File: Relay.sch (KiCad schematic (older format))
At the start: 0 parts

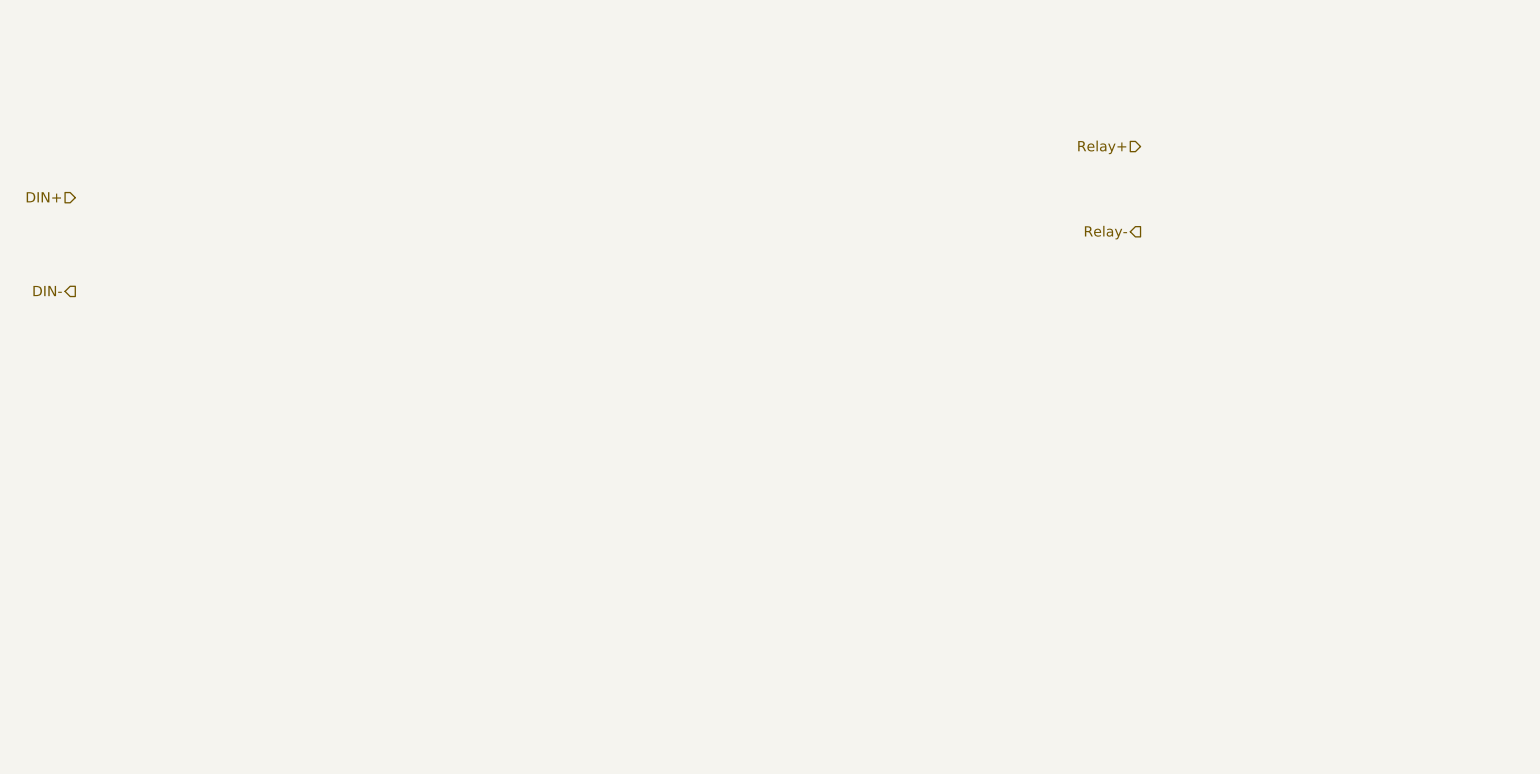
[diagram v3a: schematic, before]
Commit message: Added Relay Module Block Diagram
Everything we'll need for the relay block module, including opto and
transistor. Also created general library of schematic symbols to be used
for this project only (BenchBuddy.lib)
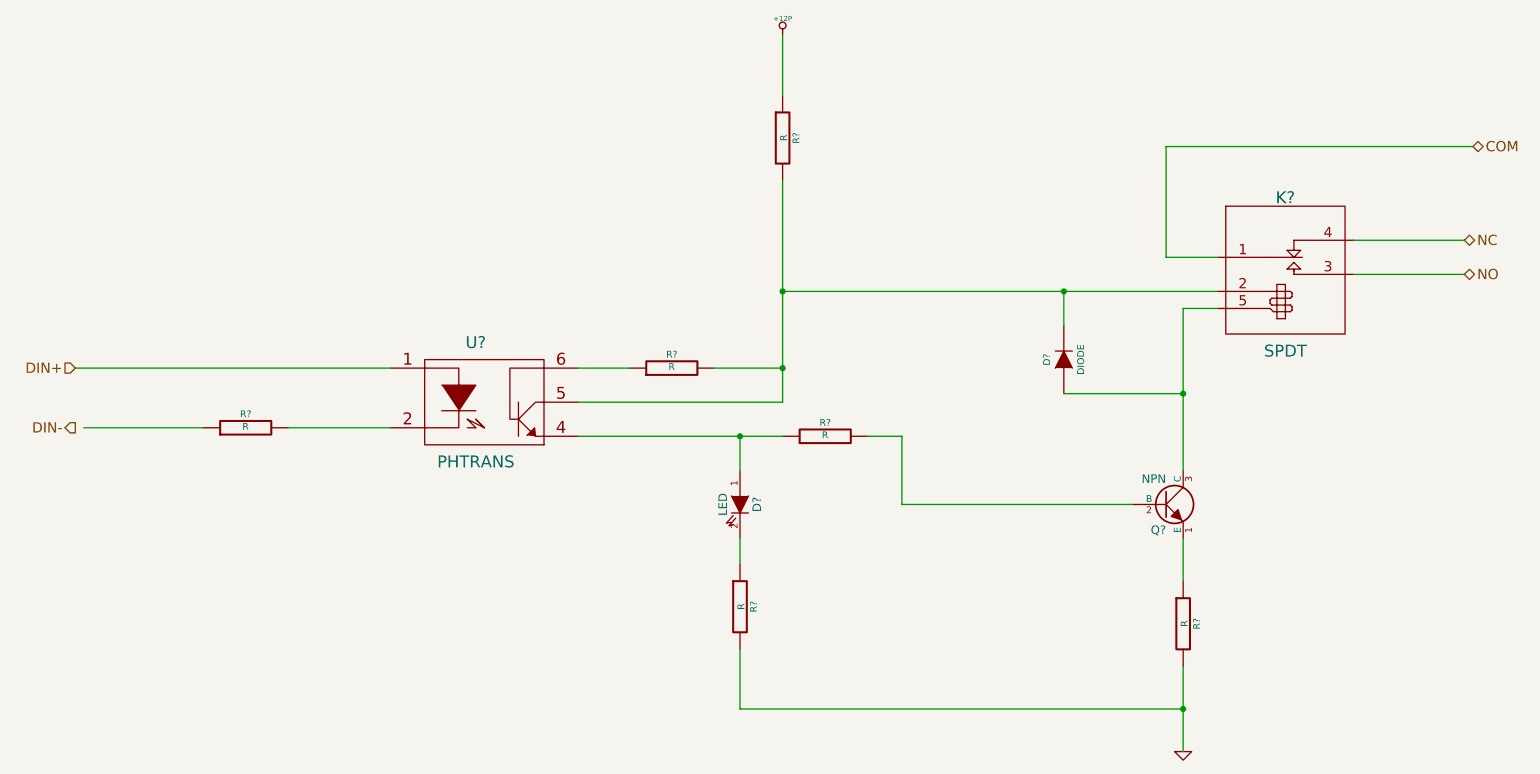
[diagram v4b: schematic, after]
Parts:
- added D?: LED, ~, symbol LED
- added D?: DIODE, ~, symbol DIODE
- added K?: SPDT, ~, symbol SPDT
- added Q?: NPN, ~, symbol NPN
- added R? (x6): R, ~, symbol R
- added U?: PHTRANS, ~, symbol PHTRANS
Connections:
- net labels added: +12P, COM, GND, NC, NO
- net labels removed: Relay+, Relay-
- wire segments 0 -> 28
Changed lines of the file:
@@
-EESchema Schematic File Version 2  date 9/16/2013 1:33:56 AM
+EESchema Schematic File Version 2  date 9/19/2013 9:09:16 PM
 LIBS:power
 LIBS:device
@@
 LIBS:contrib
 LIBS:valves
+LIBS:BenchBuddy
 LIBS:BenchBuddy-cache
 EELAYER 27 0
@@
 Sheet 4 8
 Title ""
-Date "16 sep 2013"
+Date "20 sep 2013"
 Rev ""
 Comp ""
@@
 Comment4 ""
 $EndDescr
-Text HLabel 2300 2400 0    60   Input ~ 0
+Text HLabel 2300 3400 0    60   Input ~ 0
 DIN+
-Text HLabel 2300 2950 0    60   Output ~ 0
+Text HLabel 2300 3750 0    60   Output ~ 0
 DIN-
-Text HLabel 8550 2100 0    60   Input ~ 0
-Relay+
-Text HLabel 8550 2600 0    60   Output ~ 0
-Relay-
+Text HLabel 10450 2650 2    60   BiDi ~ 0
+NC
+Text HLabel 10450 2850 2    60   BiDi ~ 0
+NO
+$Comp
+L PHTRANS U?
+U 1 1 523B9916
+P 4700 3600
+F 0 "U?" H 4650 3950 70  0000 C CNN
+F 1 "PHTRANS" H 4650 3250 70  0000 C CNN
+F 2 "~" H 4700 3600 60  0000 C CNN
+F 3 "~" H 4700 3600 60  0000 C CNN
+	1    4700 3600
+	1    0    0    -1
+$EndComp
+$Comp
+L R R?
+U 1 1 523B9943
+P 6700 3800
+F 0 "R?" V 6780 3800 40  0000 C CNN
+F 1 "R" V 6707 3801 40  0000 C CNN
+F 2 "~" V 6630 3800 30  0000 C CNN
+F 3 "~" H 6700 3800 30  0000 C CNN
+	1    6700 3800
+	0    -1   -1   0
+$EndComp
+$Comp
+L NPN Q?
+U 1 1 523B9952
+P 8700 4200
+F 0 "Q?" H 8700 4050 50  0000 R CNN
+F 1 "NPN" H 8700 4350 50  0000 R CNN
+F 2 "~" H 8700 4200 60  0000 C CNN
+F 3 "~" H 8700 4200 60  0000 C CNN
+	1    8700 4200
+	1    0    0    -1
+$EndComp
+$Comp
+L LED D?
+U 1 1 523B9961
+P 6200 4200
+F 0 "D?" H 6200 4300 50  0000 C CNN
+F 1 "LED" H 6200 4100 50  0000 C CNN
+F 2 "~" H 6200 4200 60  0000 C CNN
+F 3 "~" H 6200 4200 60  0000 C CNN
+	1    6200 4200
+	0    1    1    0
+$EndComp
+$Comp
+L SPDT K?
+U 1 1 523B9EF8
+P 9400 2700
+F 0 "K?" H 9400 3000 70  0000 C CNN
+F 1 "SPDT" H 9400 2100 70  0000 C CNN
+F 2 "~" H 9400 2700 60  0000 C CNN
+F 3 "~" H 9400 2700 60  0000 C CNN
+	1    9400 2700
+	1    0    0    -1
+$EndComp
+Text HLabel 10500 2100 2    60   BiDi ~ 0
+COM
+Wire Wire Line
+	10450 2850 9800 2850
+Wire Wire Line
+	10450 2650 9800 2650
+Wire Wire Line
+	5250 3800 6450 3800
+Wire Wire Line
+	6450 2950 9000 2950
+Wire Wire Line
+	6450 2300 6450 3600
+$Comp
+L R R?
+U 1 1 523B9FA5
+P 8800 4900
+F 0 "R?" V 8880 4900 40  0000 C CNN
+F 1 "R" V 8807 4901 40  0000 C CNN
+F 2 "~" V 8730 4900 30  0000 C CNN
+F 3 "~" H 8800 4900 30  0000 C CNN
+	1    8800 4900
+	1    0    0    -1
+$EndComp
+$Comp
+L GND #PWR?
+U 1 1 523B9FB4
+P 8800 5650
+F 0 "#PWR?" H 8800 5650 30  0001 C CNN
+F 1 "GND" H 8800 5580 30  0001 C CNN
+F 2 "" H 8800 5650 60  0000 C CNN
+F 3 "" H 8800 5650 60  0000 C CNN
+	1    8800 5650
+	1    0    0    -1
+$EndComp
+Wire Wire Line
+	8800 5150 8800 5650
+$Comp
+L R R?
+U 1 1 523B9FD6
+P 6200 4800
+F 0 "R?" V 6280 4800 40  0000 C CNN
+F 1 "R" V 6207 4801 40  0000 C CNN
+F 2 "~" V 6130 4800 30  0000 C CNN
+F 3 "~" H 6200 4800 30  0000 C CNN
+	1    6200 4800
+	1    0    0    -1
+$EndComp
+Wire Wire Line
+	6200 3800 6200 4000
+Connection ~ 6200 3800
+Wire Wire Line
+	6200 4400 6200 4550
+Wire Wire Line
+	6200 5050 6200 5400
+Wire Wire Line
+	6200 5400 8800 5400
+Connection ~ 8800 5400
+$Comp
+L R R?
+U 1 1 523BA005
+P 6450 2050
+F 0 "R?" V 6530 2050 40  0000 C CNN
+F 1 "R" V 6457 2051 40  0000 C CNN
+F 2 "~" V 6380 2050 30  0000 C CNN
+F 3 "~" H 6450 2050 30  0000 C CNN
+	1    6450 2050
+	1    0    0    -1
+$EndComp
+$Comp
+L +12P #PWR?
+U 1 1 523BA00D
+P 6450 1450
+F 0 "#PWR?" H 6450 1420 30  0001 C CNN
+F 1 "+12P" H 6450 1550 30  0000 C CNN
+F 2 "" H 6450 1450 60  0000 C CNN
+F 3 "" H 6450 1450 60  0000 C CNN
+	1    6450 1450
+	1    0    0    -1
+$EndComp
+Wire Wire Line
+	6450 1450 6450 1800
+Wire Wire Line
+	6450 3600 5250 3600
+Connection ~ 6450 2950
+$Comp
+L R R?
+U 1 1 523BA03F
+P 5800 3400
+F 0 "R?" V 5880 3400 40  0000 C CNN
+F 1 "R" V 5807 3401 40  0000 C CNN
+F 2 "~" V 5730 3400 30  0000 C CNN
+F 3 "~" H 5800 3400 30  0000 C CNN
+	1    5800 3400
+	0    -1   -1   0
+$EndComp
+Wire Wire Line
+	5550 3400 5250 3400
+Wire Wire Line
+	6050 3400 6450 3400
+Connection ~ 6450 3400
+$Comp
+L R R?
+U 1 1 523BA070
+P 3300 3750
+F 0 "R?" V 3380 3750 40  0000 C CNN
+F 1 "R" V 3307 3751 40  0000 C CNN
+F 2 "~" V 3230 3750 30  0000 C CNN
+F 3 "~" H 3300 3750 30  0000 C CNN
+	1    3300 3750
+	0    -1   -1   0
+$EndComp
+Wire Wire Line
+	3550 3750 4150 3750
+Wire Wire Line
+	2300 3400 4150 3400
+Wire Wire Line
+	2350 3750 3050 3750
+Wire Wire Line
+	10500 2100 8700 2100
+Wire Wire Line
+	8700 2100 8700 2750
+Wire Wire Line
+	8700 2750 9000 2750
+Wire Wire Line
+	9000 3050 8800 3050
+$Comp
+L DIODE D?
+U 1 1 523BA12B
+P 8100 3350
+F 0 "D?" H 8100 3450 40  0000 C CNN
+F 1 "DIODE" H 8100 3250 40  0000 C CNN
+F 2 "~" H 8100 3350 60  0000 C CNN
+F 3 "~" H 8100 3350 60  0000 C CNN
+	1    8100 3350
+	0    -1   -1   0
+$EndComp
+Wire Wire Line
+	8100 2950 8100 3150
+Connection ~ 8100 2950
+Wire Wire Line
+	8500 4200 7150 4200
+Wire Wire Line
+	7150 4200 7150 3800
+Wire Wire Line
+	7150 3800 6950 3800
+Wire Wire Line
+	8100 3550 8800 3550
+Wire Wire Line
+	8800 3050 8800 4000
+Connection ~ 8800 3550
+Wire Wire Line
+	8800 4650 8800 4400
 $EndSCHEMATC
